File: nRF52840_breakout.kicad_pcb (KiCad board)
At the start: 4 copper layers, 80 x 80 mm, 77 parts, among them J1 MM8130-2600, J2 Conn_01x12, J3 Conn_01x12, J4 Conn_01x17, J5 1734592-5, J6 Pin Header 2x5, 1.27, J7 S2B-PH-SM4-TB(LF)(SN), Q1 DMG2395, SW1 SW_Push, U1 nRF52840, U2 USB_TYPE_C, U3 AP2112K-3.3, U4 MCP73831-2-OT, Y1 32.768kHz, Y2 32MHz

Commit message: added som like version of the breakout
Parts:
- removed C1, C2: 12.5pF, Capacitor_SMD:C_0805_2012Metric_Pad1.15x1.40mm_HandSolder
- removed C26, C30, C31, C32: 10µF, Capacitor_SMD:C_0805_2012Metric_Pad1.15x1.40mm_HandSolder
- removed C27: CTUNE1, Capacitor_SMD:C_0805_2012Metric_Pad1.15x1.40mm_HandSolder
- removed C28: CTUNE2, Capacitor_SMD:C_0805_2012Metric_Pad1.15x1.40mm_HandSolder
- removed C29: 100nF, Capacitor_SMD:C_0805_2012Metric_Pad1.15x1.40mm_HandSolder
- removed D3: LED, LED_SMD:LED_0805_2012Metric_Pad1.15x1.40mm_HandSolder
- removed FB1, FB2, FB3: 120R/0.55A, Inductor_SMD:L_0805_2012Metric_Pad1.15x1.40mm_HandSolder
- removed H1, H2, H3, H4: MountingHole, MountingHole:MountingHole_2.2mm_M2_Pad_Via
- removed J6: Pin Header 2x5, 1.27, Connector_PinHeader_1.27mm:PinHeader_2x05_P1.27mm_Vertical_SMD
- removed J7: S2B-PH-SM4-TB(LF)(SN), custom_footprints:JST_PH_S2B-PH-SM4-TB_LF__SN_
- removed R10, R6, R7, R8, R9: 100k, Resistor_SMD:R_0805_2012Metric_Pad1.15x1.40mm_HandSolder
- removed R11: 5k, Resistor_SMD:R_0805_2012Metric_Pad1.15x1.40mm_HandSolder
- removed SW1: SW_Push, Button_Switch_SMD:SW_SPST_TL3342
- removed TP1: VBUS_Raw, TestPoint:TestPoint_Pad_1.0x1.0mm
- removed TP2: VBUS_nRF, TestPoint:TestPoint_Pad_1.0x1.0mm
- removed TP3: NFC1, TestPoint:TestPoint_Pad_1.0x1.0mm
- removed TP4: NFC2, TestPoint:TestPoint_Pad_1.0x1.0mm
- removed U3: AP2112K-3.3, Package_TO_SOT_SMD:SOT-23-5
- removed U4: MCP73831-2-OT, Package_TO_SOT_SMD:SOT-23-5
- C10, C11, C12, C15, C16, C17, C18, C19, C20, C21, C22, C23, C24, C3, C4, C5, C6, C7, C8, C9: footprint Capacitor_SMD:C_0805_2012Metric_Pad1.15x1.40mm_HandSolder -> Capacitor_SMD:C_0402_1005Metric
- C13, C14: value 8pF -> 6pF; footprint Capacitor_SMD:C_0805_2012Metric_Pad1.15x1.40mm_HandSolder -> Capacitor_SMD:C_0402_1005Metric
- C25: value 100nF -> NC; footprint Capacitor_SMD:C_0805_2012Metric_Pad1.15x1.40mm_HandSolder -> Capacitor_SMD:C_0402_1005Metric
- D1: value PRTR5V0U2X -> MBR120; footprint Package_TO_SOT_SMD:SOT-143 -> Diode_SMD:D_SOD-123F
- D2: value MBR120 -> LED_RED; footprint Diode_SMD:D_SOD-123F -> LED_SMD:LED_0402_1005Metric
- J1: value MM8130-2600 -> MM8930_2620; footprint custom_footprints:COAX_MM8130-2600 -> custom_footprints:MM8930_2620
- J2: value Conn_01x12 -> Conn_02x03_Odd_Even; footprint Connector_PinHeader_2.54mm:PinHeader_1x12_P2.54mm_Vertical -> Connector:Tag-Connect_TC2030-IDC-NL_2x03_P1.27mm_Vertical
- J3: value Conn_01x12 -> Conn_01x22; footprint Connector_PinHeader_2.54mm:PinHeader_1x12_P2.54mm_Vertical -> Connector_PinHeader_1.27mm:PinHeader_1x22_P1.27mm_Vertical
- J4: value Conn_01x17 -> Conn_01x16; footprint Connector_PinHeader_2.54mm:PinHeader_1x17_P2.54mm_Vertical -> Connector_PinHeader_1.27mm:PinHeader_1x16_P1.27mm_Vertical
- J5: value 1734592-5 -> Conn_01x22; footprint custom_footprints:CONNECTOR_FFC_1734592-5 -> Connector_PinHeader_1.27mm:PinHeader_1x22_P1.27mm_Vertical
- L1: value 10µH -> NC; footprint Inductor_SMD:L_0805_2012Metric_Pad1.15x1.40mm_HandSolder -> Inductor_SMD:L_0402_1005Metric
- L2, L3, L4: footprint Inductor_SMD:L_0805_2012Metric_Pad1.15x1.40mm_HandSolder -> Inductor_SMD:L_0402_1005Metric
- R1, R2: value 5.1k -> 100k; footprint Resistor_SMD:R_0805_2012Metric_Pad1.15x1.40mm_HandSolder -> Resistor_SMD:R_0402_1005Metric
- R3: value 22 -> 1k; footprint Resistor_SMD:R_0805_2012Metric_Pad1.15x1.40mm_HandSolder -> Resistor_SMD:R_0402_1005Metric
- R4: value 22 -> NC; footprint Resistor_SMD:R_0805_2012Metric_Pad1.15x1.40mm_HandSolder -> Resistor_SMD:R_0402_1005Metric
- R5: value 10k -> 0R; footprint Resistor_SMD:R_0805_2012Metric_Pad1.15x1.40mm_HandSolder -> Resistor_SMD:R_0402_1005Metric
- U2: value USB_TYPE_C -> AP2112K-3.3; footprint custom_footprints:USB_C_Receptacle_Amphenol_12401610E4-2A -> Package_TO_SOT_SMD:SOT-23-5
- Y1: value 32.768kHz -> 32.768kHz-SIT1533AI-H4-DCC-32.768E; footprint Crystal:Crystal_SMD_3215-2Pin_3.2x1.5mm -> Crystal:Crystal_SMD_2012-2Pin_2.0x1.2mm
- Y2: value 32MHz -> 32MHz-XRCGB32M000F1H00R0; footprint Crystal:Crystal_SMD_5032-2Pin_5.0x3.2mm_HandSoldering -> Crystal:Crystal_SMD_2016-4Pin_2.0x1.6mm
- moved J5 47.0 mm to (123.2, 54.6)
- moved J4 44.2 mm to (101.6, 53.3), turned to 90 degrees
- moved J2 42.4 mm to (119.8, 75.8), turned to 90 degrees
- moved R2 40.4 mm to (114.9, 60.5), turned to 180 degrees
- moved U2 38.2 mm to (115.6, 58.0), turned to 90 degrees
- moved R3 37.8 mm to (119.5, 60.0), turned to 180 degrees
- moved D1 30.1 mm to (110.5, 60.7), turned to 180 degrees
- moved R5 28.7 mm to (103.6, 69.0), turned to 45 degrees
- moved C24 27.8 mm to (118.0, 58.5), turned to 270 degrees
- moved C23 26.5 mm to (113.3, 61.1), turned to 270 degrees
- moved AE1 26.4 mm to (115.7, 82.0), turned to 180 degrees
- moved R1 25.9 mm to (109.2, 58.4), turned to 270 degrees
- moved R4 24.2 mm to (102.0, 70.3), turned to 180 degrees
- moved C22 24.0 mm to (116.2, 80.5), turned to 0 degrees
- moved C25 23.7 mm to (101.6, 71.8), turned to 270 degrees
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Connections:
- C24 pad 1: Net-(C23-Pad1) -> VDD_nRF
- C25 pad 1: Net-(C23-Pad1) -> VDDH
- D1 pad 1: GND -> Net-(C23-Pad1)
- D1 pad 2: Net-(D1-Pad2) -> VBUS_nRF
- D2 pad 1: Net-(C30-Pad1) -> GND
- D2 pad 2: VBUS_nRF -> Net-(D2-Pad2)
- J2 pad 1: P0.26 -> P1.00_SWO
- J2 pad 2: P0.27 -> P1.18_RESET
- J2 pad 3: P0.04_AIN2 -> SWDIO
- J2 pad 4: P0.05_AIN3 -> GND
- J2 pad 5: P0.06 -> SWDCLK
- J2 pad 6: P0.07 -> VDD_nRF
- J3 pad 1: P0.14 -> GND
- J3 pad 10: P0.24 -> P0.19
- J3 pad 11: P0.25 -> P0.17
- J3 pad 12: P1.01 -> P0.16
- J3 pad 2: P0.15 -> VDD_nRF
- J3 pad 3: P0.16 -> P0.25
- J3 pad 4: P0.17 -> P0.24
- J3 pad 5: P0.19 -> P0.23
- J3 pad 6: P0.20 -> P0.22
- J3 pad 8: P0.22 -> P0.20
- J3 pad 9: P0.23 -> VDDH
- J4 pad 1: P1.02 -> P0.07
- J4 pad 10: P1.13 -> VBUS_nRF
- J4 pad 11: P1.14 -> VDD_BAT
- J4 pad 12: P1.15 -> P0.31_AIN7
- J4 pad 13: P0.03_AIN1 -> P0.30_AIN6
- J4 pad 14: P0.02_AIN0 -> P0.29_AIN5
- J4 pad 16: P0.29_AIN5 -> P0.02_AIN0
- J4 pad 2: P1.03 -> P0.06
- J4 pad 3: P1.04 -> P0.05_AIN3
- J4 pad 4: P1.05 -> P0.04_AIN2
- J4 pad 5: P1.06 -> P0.27
- J4 pad 6: P1.07 -> P0.26
- J4 pad 7: P1.10 -> GND
- J4 pad 8: P1.11 -> D+
- J4 pad 9: P1.12 -> D-
- J5 pad 1: Net-(J5-Pad1) -> GND
- J5 pad 2: P0.09_NFC1 -> VDD_nRF
- J5 pad 3: Net-(J5-Pad3) -> P1.15
- J5 pad 4: P0.10_NFC2 -> P1.14
- J5 pad 5: Net-(J5-Pad5) -> P1.13
- Q1 pad 3: Net-(C30-Pad1) -> Net-(C23-Pad1)
- R1 pad 2: Net-(R1-Pad2) -> VBUS_nRF
- R2 pad 1: GND -> Net-(R2-Pad1)
- R2 pad 2: Net-(R2-Pad2) -> Net-(C23-Pad1)
- R3 pad 1: D- -> VDD_nRF
- R3 pad 2: Net-(D1-Pad2) -> Net-(D2-Pad2)
- R4 pad 1: Net-(D1-Pad3) -> Net-(R4-Pad1)
- R4 pad 2: D+ -> VDDH
- R5 pad 1: VDD_nRF -> Net-(R4-Pad1)
- R5 pad 2: P1.18_RESET -> VDD_nRF
- U1 pad Y2: VDD_nRF -> Net-(R4-Pad1)
- Y2 pad 1: Net-(C14-Pad2) -> GND
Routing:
- net VBUS_nRF: track 91.8 -> 12.4 mm, vias 2 -> 0
- net VDD_nRF: track 88.3 -> 25.6 mm, vias 8 -> 0
- net Net-(C23-Pad1): track 44.8 -> 6.02 mm
- net P0.30_AIN6: track 55.1 -> 17.8 mm
- net P0.29_AIN5: track 51.7 -> 17.9 mm
- net P1.18_RESET: track 63.9 -> 30.4 mm, vias 4 -> 2
- net VDD_BAT: track 37.2 -> 4.00 mm
- net P0.28_AIN4: track 50.0 -> 19.1 mm
- net P0.02_AIN0: track 48.6 -> 19.4 mm
- net Net-(C19-Pad1): track 45.8 -> 17.9 mm
- net P1.15: track 44.2 -> 17.5 mm
- net Net-(D1-Pad2): track 26.2 -> 0.00 mm, vias 2 -> 0
- net P1.14: track 43.1 -> 16.9 mm, vias 1 -> 2
- net P1.13: track 41.0 -> 15.5 mm
- net Net-(FB2-Pad2): track 24.9 -> 0.00 mm
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- removed copper zone on B.Cu, net GND
- removed copper zone on F.Cu, net GND
- removed copper zone on In1.Cu, net GND
- removed copper zone on In2.Cu, net VDD_nRF
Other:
- board size 80 x 80 mm -> 24.1 x 34.3 mm
- net class custom: via_dia 0.61 -> 0.45; via_drill 0.305 -> 0.2
- rule via_min_drill: 0.3 -> 0.2
- rule via_min_size: 0.4 -> 0.45

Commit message: path selection/charging/bme680 sensor integration
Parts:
- removed Q1: DMG2395, Package_TO_SOT_SMD:SOT-23
- added C1: 10µF, Capacitor_SMD:C_0402_1005Metric, F.Cu at (113.4, 56.3)
- added C2: 10µF, Capacitor_SMD:C_0402_1005Metric, F.Cu at (114.0, 59.6)
- added C26: 0.1µF, Capacitor_SMD:C_0402_1005Metric, F.Cu at (118.5, 61.5)
- added C27: 10µF, Capacitor_SMD:C_0402_1005Metric, F.Cu at (121.0, 58.1)
- added C28: 100nF, Capacitor_SMD:C_0402_1005Metric, F.Cu at (104.8, 55.5)
- added C29: 100nF, Capacitor_SMD:C_0402_1005Metric, F.Cu at (107.1, 57.1)
- added J6: S2B-PH-SM4-TB(LF)(SN), custom_footprints:JST_PH_S2B-PH-SM4-TB_LF__SN_, B.Cu at (117.1, 62.0)
- added J7: Conn_Coaxial, custom_footprints:MM8930_2620, F.Cu at (112.9, 80.3)
- added L5: L_Small, Inductor_SMD:L_0402_1005Metric, F.Cu at (118.5, 56.4)
- added R10: 4.7k, Resistor_SMD:R_0402_1005Metric, F.Cu at (105.7, 61.1)
- added R11: 0R, Resistor_SMD:R_0402_1005Metric, F.Cu at (115.7, 80.7)
- added R12: 0R, Resistor_SMD:R_0402_1005Metric, F.Cu at (115.2, 79.2)
- added R6: 10k, Resistor_SMD:R_0402_1005Metric, F.Cu at (108.0, 57.8)
- added R7: 1.5k, Resistor_SMD:R_0402_1005Metric, F.Cu at (115.1, 63.0)
- added R8: 1.5k, Resistor_SMD:R_0402_1005Metric, F.Cu at (115.1, 61.9)
- added R9: 4.7k, Resistor_SMD:R_0402_1005Metric, F.Cu at (105.7, 60.0)
- added U3: TPS63031, Package_SON:Texas_DRC0010J_ThermalVias, F.Cu at (118.5, 59.0)
- added U4: BME680, Package_LGA:Bosch_LGA-8_3x3mm_P0.8mm_ClockwisePinNumbering, F.Cu at (104.8, 57.7)
- D1: value MBR120 -> GRN; footprint Diode_SMD:D_SOD-123F -> LED_SMD:LED_0402_1005Metric
- D2: value LED_RED -> RED
- R1: value 100k -> 46.4k
- R2: value 100k -> 1.18k
- R3: value 1k -> 1.13k
- U2: value AP2112K-3.3 -> BQ24072; footprint Package_TO_SOT_SMD:SOT-23-5 -> Package_DFN_QFN:VQFN-16-1EP_3x3mm_P0.5mm_EP1.68x1.68mm_ThermalVias
- moved R3 11.2 mm to (108.9, 56.3)
- moved D2 6.44 mm to (113.1, 61.9), turned to 0 degrees
- moved C23 5.41 mm to (108.0, 59.8)
- moved U2 4.98 mm to (110.8, 59.2), turned to 0 degrees
- moved J1 3.65 mm to (112.9, 75.8), turned to 45 degrees
- moved D1 3.46 mm to (113.1, 63.0), turned to 0 degrees
- moved R2 3.12 mm to (113.9, 57.5), turned to 0 degrees
- moved R1 2.70 mm to (110.9, 56.3), turned to 180 degrees
- moved C17 2.46 mm to (115.0, 76.5)
- moved L4 2.03 mm to (114.3, 77.3)
- moved C24 2.00 mm to (116.0, 58.5)
- moved C20 1.85 mm to (116.1, 77.6)
- moved C22 1.22 mm to (116.2, 79.2)
- moved C21 1.22 mm to (113.4, 78.4), turned to 0 degrees
- moved C15 0.36 mm to (111.6, 77.1)
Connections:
- C22 pad 1: Net-(AE1-Pad1) -> Net-(C20-Pad2)
- C23 pad 1: Net-(C23-Pad1) -> VDD_BAT
- C24 pad 1: VDD_nRF -> V_SYS
- D1 pad 1: Net-(C23-Pad1) -> Net-(D1-Pad1)
- D1 pad 2: VBUS_nRF -> Net-(D1-Pad2)
- D2 pad 1: GND -> Net-(D2-Pad1)
- J1 pad 1: Net-(C20-Pad2) -> Net-(J1-Pad1)
- J1 pad 2: Net-(AE1-Pad1) -> Net-(C17-Pad2)
- J2 pad 1: P1.00_SWO -> VDD_nRF
- J2 pad 2: P1.18_RESET -> SWDIO
- J2 pad 3: SWDIO -> P1.18_RESET
- J2 pad 4: GND -> SWDCLK
- J2 pad 5: SWDCLK -> GND
- J2 pad 6: VDD_nRF -> P1.00_SWO
- J3 pad 18: P0.09_NFC1 -> P0.10_NFC2
- J3 pad 19: P0.10_NFC2 -> P0.09_NFC1
- R1 pad 1: GND -> Net-(R1-Pad1)
- R1 pad 2: VBUS_nRF -> GND
- R2 pad 2: Net-(C23-Pad1) -> GND
- R3 pad 1: VDD_nRF -> Net-(R3-Pad1)
- R3 pad 2: Net-(D2-Pad2) -> GND
- U1 pad H23: Net-(C17-Pad2) -> Net-(J1-Pad1)
- U2 pad 1: Net-(C23-Pad1) -> Net-(R6-Pad2)
- U2 pad 2: GND -> VDD_BAT
- U2 pad 3: Net-(R2-Pad1) -> VDD_BAT
- U2 pad 4: Net-(U2-Pad4) -> GND
- U2 pad 5: VDD_nRF -> P0.27
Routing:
- net VDD_BAT: track 4.00 -> 22.1 mm, vias 0 -> 1
- net P1.09: track 27.3 -> 33.9 mm, vias 2 -> 3
- net P1.08: track 26.9 -> 33.6 mm, vias 2 -> 3
- net VDDIO: track 0.00 -> 6.40 mm
- net Net-(C23-Pad1): track 6.02 -> 0.00 mm
- net VDD_nRF: track 25.6 -> 19.7 mm
- net V_SYS: track 0.00 -> 4.81 mm
- net VBUS_nRF: track 12.4 -> 7.80 mm
- net D-: track 25.7 -> 30.2 mm
- net D+: track 26.4 -> 30.6 mm
- net P1.00_SWO: track 22.5 -> 26.5 mm, vias 1 -> 3
- net Net-(J1-Pad1): track 0.00 -> 3.75 mm
- net P0.09_NFC1: track 26.4 -> 30.1 mm, vias 1 -> 3
- net Net-(D1-Pad1): track 0.00 -> 3.02 mm
- net Net-(C17-Pad2): track 4.19 -> 1.76 mm
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
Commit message: changes
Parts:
- removed J1: MM8930_2620, custom_footprints:MM8930_2620
- added U5: MM8130-2600RA2, custom_footprints:MM8930_2620, F.Cu at (112.8, 75.9)
- J7: footprint custom_footprints:MM8930_2620 -> custom_footprints:CON_AMP_A-1JB
- Y1: value 32.768kHz-SIT1533AI-H4-DCC-32.768E -> SiT1533; footprint Crystal:Crystal_SMD_2012-2Pin_2.0x1.2mm -> custom_footprints:Crystal_SMD_2012-4Pin_2.2mmx1.4mm
- moved J7 5.02 mm to (108.0, 79.3), turned to 90 degrees
- moved C16 3.03 mm to (104.5, 78.1), turned to 180 degrees
- moved Y1 0.57 mm to (106.1, 64.9), turned to 45 degrees
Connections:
- Y1 pad 1: Net-(U1-PadD2) -> Net-(U1-PadF2)
- Y1 pad 2: Net-(U1-PadF2) -> GND
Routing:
- net VDD_nRF: track 19.7 -> 24.4 mm
- net Net-(J7-Pad1): track 1.65 -> 5.48 mm
- net GND: track 4.00 -> 4.82 mm, vias 22 -> 23
- net P1.00_SWO: track 26.5 -> 25.8 mm
- net Net-(U1-PadD2): track 3.89 -> 4.48 mm

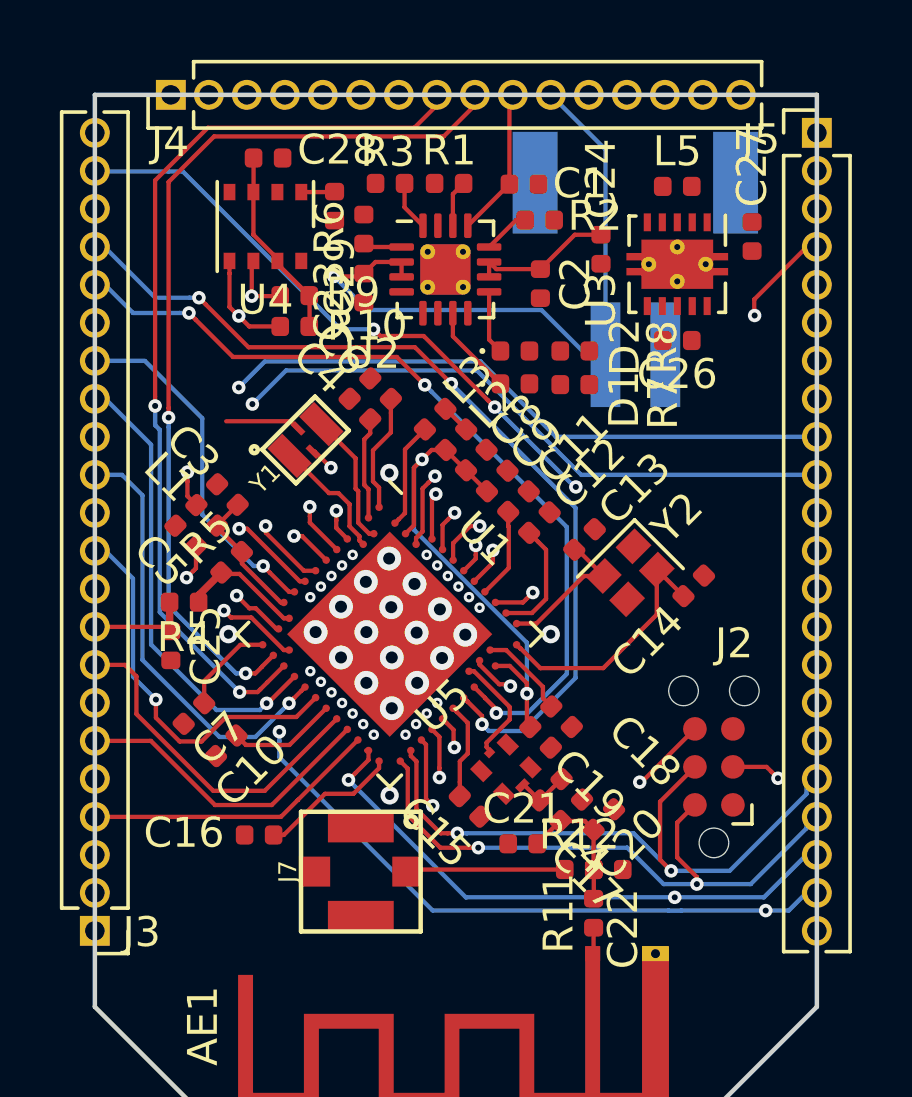
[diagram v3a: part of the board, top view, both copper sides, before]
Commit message: minor changes / switched from tag - 10pol debug connector
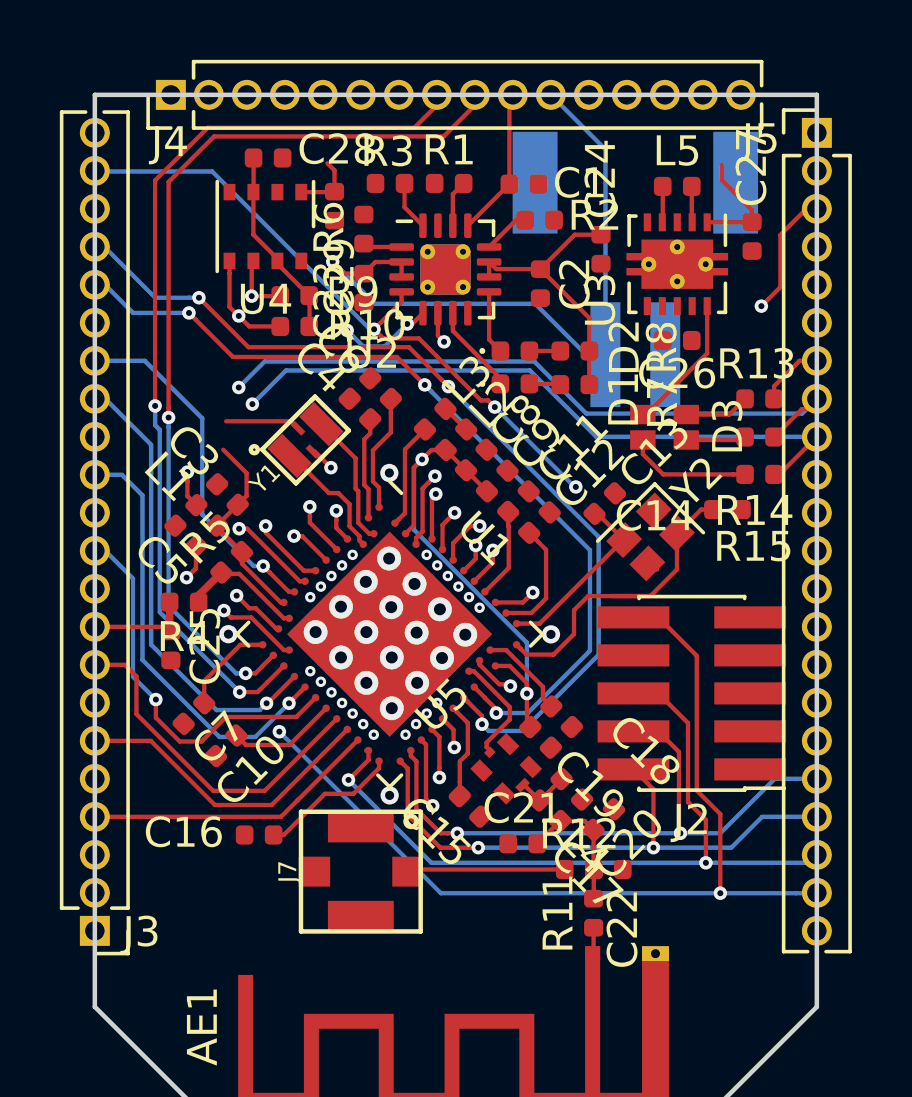
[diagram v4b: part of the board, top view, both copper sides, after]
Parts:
- added D3: LTST-C19HE1WT, custom_footprints:LTST-C19HE1WT, F.Cu at (118.4, 65.3)
- added R13: 1.5k, Resistor_SMD:R_0402_1005Metric, F.Cu at (121.3, 63.5)
- added R14: 1.5k, Resistor_SMD:R_0402_1005Metric, F.Cu at (121.3, 64.8)
- added R15: 1.5k, Resistor_SMD:R_0402_1005Metric, F.Cu at (121.3, 66.0)
- J2: value Conn_02x03_Odd_Even -> Conn_ARM_JTAG_SWD_10; footprint Connector:Tag-Connect_TC2030-IDC-NL_2x03_P1.27mm_Vertical -> Connector_PinHeader_1.27mm:PinHeader_2x05_P1.27mm_Vertical_SMD
- L5: value L_Small -> 1.5µH
- moved C14 2.79 mm to (120.2, 67.2), turned to 180 degrees
- moved J2 2.57 mm to (119.0, 73.3), turned to 180 degrees
- moved C13 1.38 mm to (116.1, 67.0)
- moved Y2 1.38 mm to (117.6, 68.1)
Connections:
- J2 pad 3: P1.18_RESET -> GND
- J5 pad 10: P1.08 -> P1.07
- J5 pad 11: P1.07 -> P1.06
- J5 pad 12: P1.06 -> P1.05
- J5 pad 13: P1.05 -> P1.04
- J5 pad 14: P1.04 -> P1.03
- J5 pad 15: P1.03 -> P1.02
- J5 pad 16: P1.02 -> P1.01
- J5 pad 17: P1.01 -> VDD_nRF
- J5 pad 2: VDD_nRF -> P1.15
- J5 pad 3: P1.15 -> P1.14
- J5 pad 4: P1.14 -> P1.13
- J5 pad 5: P1.13 -> P1.12
- J5 pad 6: P1.12 -> P1.11
- J5 pad 7: P1.11 -> P1.10
- J5 pad 8: P1.10 -> P1.09
- J5 pad 9: P1.09 -> P1.08
- U2 pad 4: GND -> P0.03_AIN1
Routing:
- net VDD_nRF: track 24.4 -> 36.1 mm
- net P0.26: track 15.0 -> 20.0 mm, vias 1 -> 2
- net V_SYS: track 4.81 -> 9.35 mm
- net P1.18_RESET: track 29.4 -> 33.9 mm, vias 4 -> 3
- net Net-(D3-Pad3): track 0.00 -> 4.17 mm
- net P0.27: track 16.2 -> 19.3 mm, vias 1 -> 3
- net Net-(C14-Pad2): track 8.51 -> 11.2 mm
- net P1.10: track 13.2 -> 15.6 mm
- net Net-(D3-Pad1): track 0.00 -> 2.18 mm
- net P1.01: track 19.8 -> 17.8 mm
- net Net-(D3-Pad2): track 0.00 -> 2.01 mm
- net P0.03_AIN1: track 25.6 -> 27.2 mm
- net SWDIO: track 20.5 -> 19.0 mm
- net P1.14: track 16.9 -> 18.2 mm
- net Net-(L5-Pad2): track 0.00 -> 1.21 mm
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
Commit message: layout / added part details etc
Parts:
- AE1: value Antenna -> Antenna_Shield
- moved C14 1.99 mm to (119.3, 69.0)
- moved C13 1.66 mm to (115.7, 65.4), turned to 315 degrees
- moved Y2 0.75 mm to (117.1, 67.6), turned to 135 degrees
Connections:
- AE1 pad 2: (no net) -> GND
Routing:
- net VBUS_nRF: track 7.80 -> 39.1 mm, vias 0 -> 3
- net GND: track 4.83 -> 32.1 mm, vias 23 -> 84
- net VDD_nRF: track 36.1 -> 59.5 mm, vias 0 -> 15
- net Net-(C14-Pad2): track 11.2 -> 8.27 mm
- net Net-(C13-Pad2): track 6.10 -> 8.07 mm
- net V_SYS: track 9.35 -> 11.1 mm
- net P0.03_AIN1: track 27.2 -> 28.2 mm
- net P0.28_AIN4: track 19.1 -> 19.7 mm
- net P0.09_NFC1: track 30.6 -> 30.0 mm
- net P0.10_NFC2: track 28.4 -> 27.8 mm
- added copper zone on F.Cu, net GND
- added copper zone on In1.Cu, net GND
- added copper zone on In2.Cu, net GND
- added copper zone on F.Cu, net Net-(C26-Pad1)
- added copper zone on F.Cu, net VDD_BAT
- added copper zone on B.Cu, net VDD_nRF
- added copper zone on F.Cu, net VDD_nRF
- added copper zone on F.Cu, net V_SYS
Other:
- net class RF added: clearance 0.3, trace_width 0.35, via_dia 0.6, via_drill 0.3
- net class VDD_BAT added: clearance 0.2, trace_width 0.35, via_dia 0.6, via_drill 0.3
- net class VDD_H added: clearance 0.2, trace_width 0.3, via_dia 0.6, via_drill 0.3
- net class VDD_nRF added: clearance 0.2, trace_width 0.3, via_dia 0.6, via_drill 0.3
